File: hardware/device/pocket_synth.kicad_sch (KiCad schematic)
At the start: 7 parts

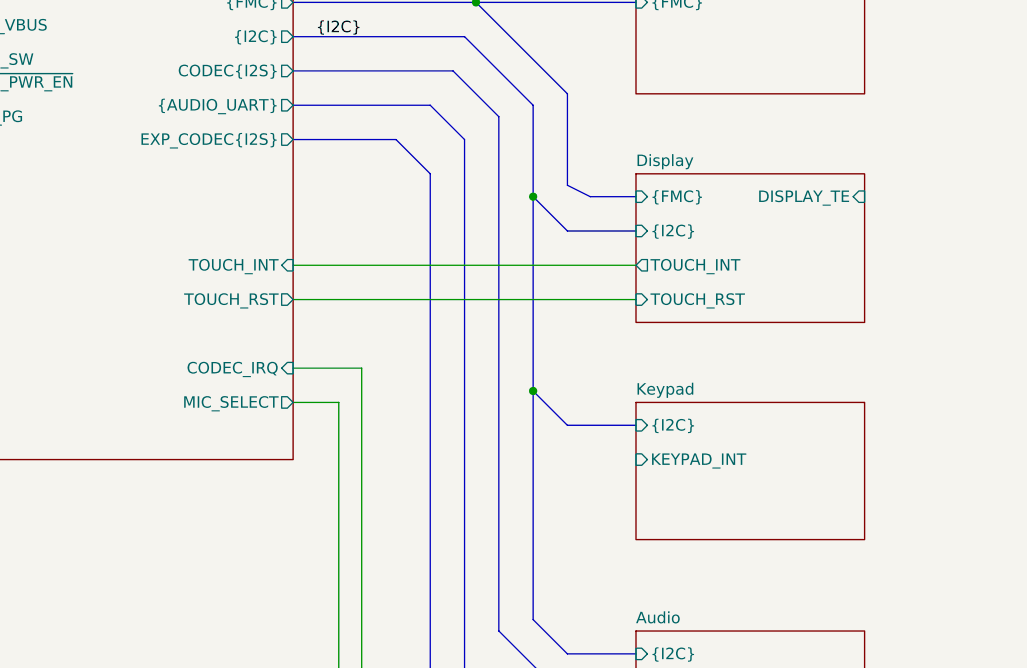
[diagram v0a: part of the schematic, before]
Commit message: feat: add SWD connector, route bluetooth, route velocity matrix
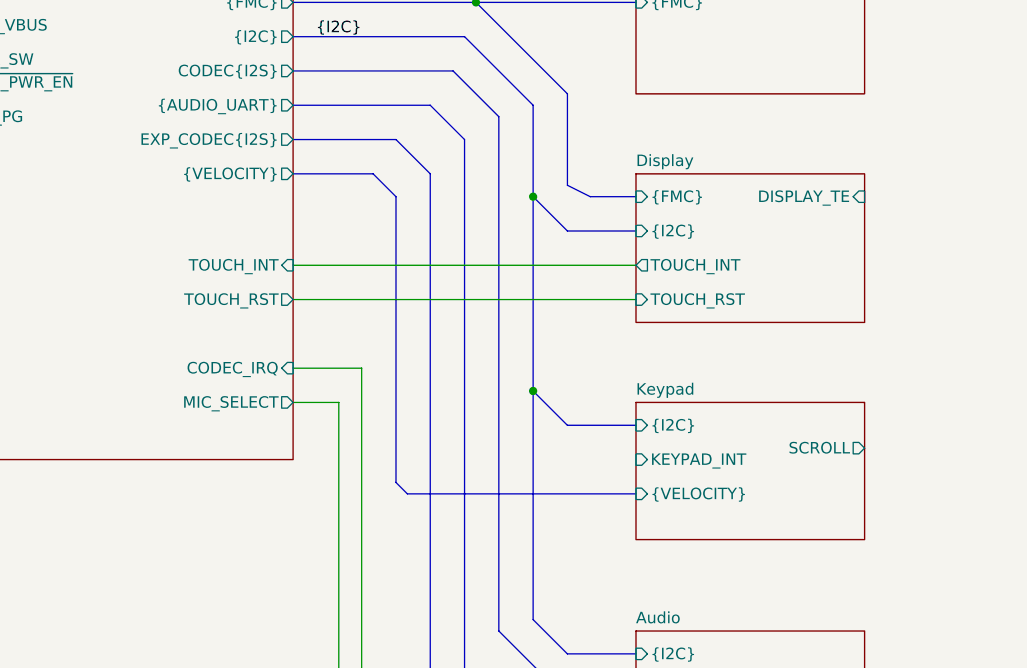
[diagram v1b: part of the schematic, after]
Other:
- sheet Keypad ports: added SCROLL, {VELOCITY}; removed none
- sheet MCU ports: added {VELOCITY}; removed none
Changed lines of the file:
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@@
 		(members "MCLK" "ADCDAT" "DACDAT" "LRCLK" "BCLK")
+	)
+	(bus_alias "VELOCITY"
+		(members "ROW0" "ROW1" "ROW2" "ROW3" "COL0" "COL1" "COL2" "COL3")
 	)
 	(text "1MOhm resistor provides protection\nagainst ESD from the metal case."
@@
 		)
 	)
+	(bus
+		(pts
+			(xy 113.03 97.79) (xy 114.3 99.06)
+		)
+		(stroke
+			(width 0)
+			(type default)
+		)
+	)
 	(wire
 		(pts
@@
 		(pts
 			(xy 101.6 40.64) (xy 139.7 40.64)
+		)
+		(stroke
+			(width 0)
+			(type default)
+		)
+	)
+	(bus
+		(pts
+			(xy 113.03 66.04) (xy 113.03 97.79)
 		)
 		(stroke
@@
 	(bus
 		(pts
+			(xy 101.6 63.5) (xy 110.49 63.5)
+		)
+		(stroke
+			(width 0)
+			(type default)
+		)
+	)
+	(bus
+		(pts
 			(xy 132.08 54.61) (xy 132.08 64.77)
 		)
@@
 		(pts
 			(xy 101.6 55.88) (xy 116.84 55.88)
+		)
+		(stroke
+			(width 0)
+			(type default)
+		)
+	)
+	(bus
+		(pts
+			(xy 114.3 99.06) (xy 139.7 99.06)
+		)
+		(stroke
+			(width 0)
+			(type default)
+		)
+	)
+	(bus
+		(pts
+			(xy 110.49 63.5) (xy 113.03 66.04)
 		)
 		(stroke
@@
 			)
 		)
+		(pin "{VELOCITY}" output
+			(at 101.6 63.5 0)
+			(effects
+				(font
+					(size 1.27 1.27)
+				)
+				(justify right)
+			)
+		)
 		(instances
 			(project "pocket_synth"
@@
 			(effects
 				(font
+					(size 1.27 1.27)
+				)
+				(justify left)
+			)
+		)
+		(pin "SCROLL" output
+			(at 165.1 93.98 0)
+			(effects
+				(font
+					(size 1.27 1.27)
+				)
+				(justify right)
+			)
+		)
+		(pin "{VELOCITY}" input
+			(at 139.7 99.06 180)
+			(effects
+				(font
